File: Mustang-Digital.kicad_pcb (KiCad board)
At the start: 2 copper layers, 67 x 93.3 mm, 100 parts, among them J302 Conn_01x02_Socket, J303 2130830005, J7 Conn_02x08_Odd_Even, J8 Conn_02x08_Odd_Even, U1 BM83SM1-00TB, U2 LP5012RUKR, U301 SPU03L-05, U302 SPU03L-05, U303 SPU03L-05, U304 ADUM4160BRWZ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

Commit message: 3D models.
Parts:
- added J1: 685119248123, Mustang_Library:685119248123, F.Cu at (107.0, 42.7)
- added J2: 685119248123, Mustang_Library:685119248123, F.Cu at (94.2, 42.7)
- C142, C143, C144, C145, D1, D2, D3, D4, D5, D6, D7, D8, U2: moved to B.Cu
- moved J7 223.4 mm to (93.0, 82.2)
- moved U301 223.4 mm to (138.2, 110.1)
- moved C301 223.4 mm to (121.3, 111.0)
- moved C302 223.4 mm to (124.3, 111.0)
- moved C303 223.4 mm to (122.7, 92.3)
- moved C310 223.4 mm to (136.8, 88.0)
- moved C311 223.4 mm to (144.3, 88.0)
- moved L302 223.4 mm to (136.8, 91.0)
- moved L303 223.4 mm to (144.3, 91.0)
- moved R303 223.4 mm to (126.7, 89.8)
- moved R304 223.4 mm to (129.7, 89.8)
- moved R307 223.4 mm to (122.7, 89.3)
- moved R308 223.4 mm to (122.7, 86.3)
- moved S1 223.4 mm to (95.3, 66.8)
- moved S3 223.4 mm to (140.7, 47.2)
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
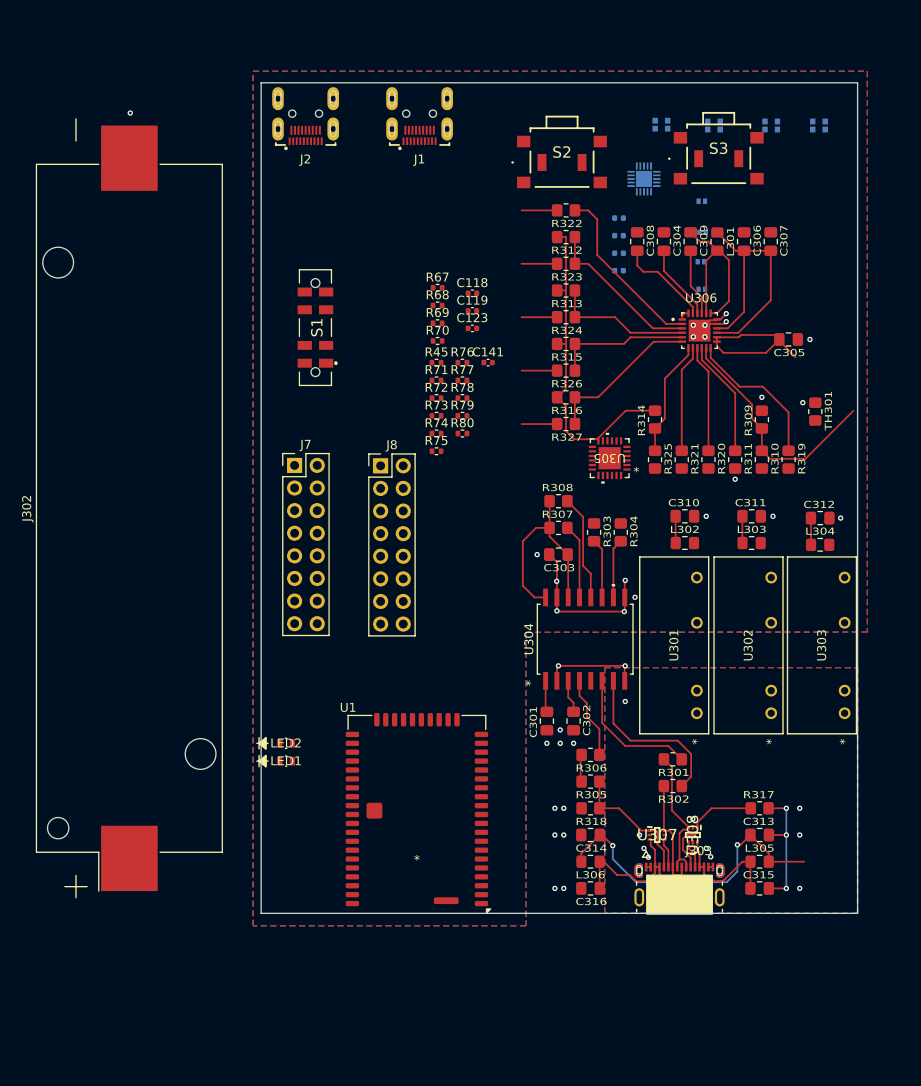
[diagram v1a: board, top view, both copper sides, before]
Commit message: Place and align PCB components to enclosure DXF. Expand PCB 15mm both sides of USB-C. Move BM83 to right side. Cutout PCB along right side for antenna function.
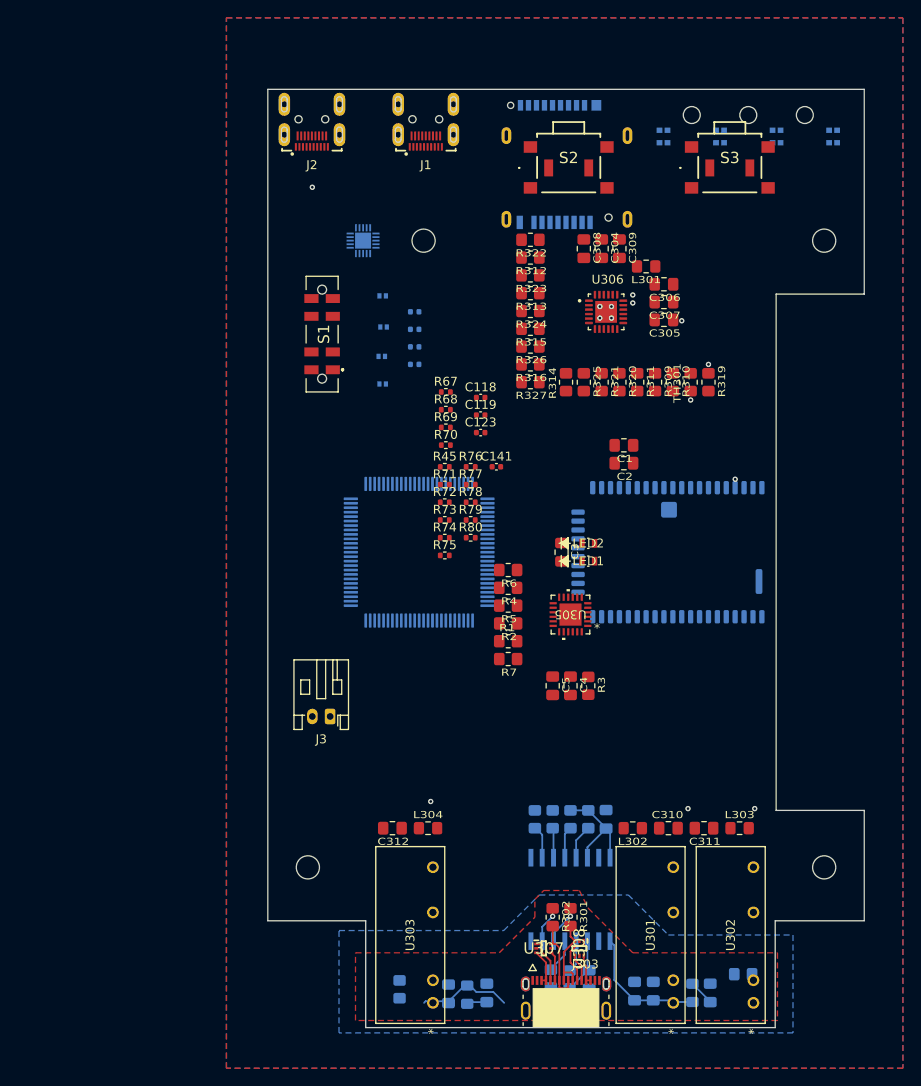
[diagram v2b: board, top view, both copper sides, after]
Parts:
- removed J302: Conn_01x02_Socket, Mustang_Library:BatteryHolder_Keystone_1042_1x18650
- removed J7, J8: Conn_02x08_Odd_Even, Connector_PinHeader_2.54mm:PinHeader_2x08_P2.54mm_Vertical
- added C1: 0.1uF, Mustang_Library:C_0805_2012Metric_Pad1.18x1.45mm_HandSolder, F.Cu at (130.0, 80.0)
- added C2: 1uF, Mustang_Library:C_0805_2012Metric_Pad1.18x1.45mm_HandSolder, F.Cu at (130.0, 82.0)
- added C3: 1uF, Mustang_Library:C_0805_2012Metric_Pad1.18x1.45mm_HandSolder, F.Cu at (123.0, 92.0)
- added C4: 18pF, Mustang_Library:C_0805_2012Metric_Pad1.18x1.45mm_HandSolder, F.Cu at (124.0, 107.0)
- added C5: 18pF, Mustang_Library:C_0805_2012Metric_Pad1.18x1.45mm_HandSolder, F.Cu at (122.0, 107.0)
- added J3: Conn_01x02_Pin, Mustang_Library:JST_PH_S2B-PH-K_1x02_P2.00mm_Horizontal, F.Cu at (97.0, 110.5)
- added J4: Micro_SD_Card_4.0_CUI, Mustang_Library:microSD_XC_CUI_MSD4-1-A, B.Cu at (123.6, 45.2)
- added MECH1: Light_Pipe_LEDs, Mustang_Library:Light_Pipe_LEDs, B.Cu at (144.0, 37.4)
- added MH1: Mounting_Holes, Mustang_Library:Mounting_Holes, F.Cu at (90.0, 40.0)
- added R1: 100k, Mustang_Library:R_0805_2012Metric_Pad1.20x1.40mm_HandSolder, F.Cu at (117.0, 102.0)
- added R2: 100k, Mustang_Library:R_0805_2012Metric_Pad1.20x1.40mm_HandSolder, F.Cu at (117.0, 100.0)
- added R3: 12k, Mustang_Library:R_0805_2012Metric_Pad1.20x1.40mm_HandSolder, F.Cu at (126.0, 107.0)
- added R4: 24R, Mustang_Library:R_0805_2012Metric_Pad1.20x1.40mm_HandSolder, F.Cu at (117.0, 96.0)
- added R5: 24R, Mustang_Library:R_0805_2012Metric_Pad1.20x1.40mm_HandSolder, F.Cu at (117.0, 98.0)
- added R6: 24R, Mustang_Library:R_0805_2012Metric_Pad1.20x1.40mm_HandSolder, F.Cu at (117.0, 94.0)
- added R7: 24R, Mustang_Library:R_0805_2012Metric_Pad1.20x1.40mm_HandSolder, F.Cu at (117.0, 104.0)
- added U3: STM32L496VGTx, Mustang_Library:LQFP-100_14x14mm_P0.5mm, B.Cu at (107.0, 92.0)
- C301, C302, C303, C313, C314, C315, C316, L305, L306, R303, R304, R305, R306, R307, R308, R317, R318, U1, U304: moved to B.Cu
- moved C312 59.3 mm to (104.0, 123.0), turned to 0 degrees
- moved U303 56.5 mm to (108.5, 142.6)
- moved L304 54.3 mm to (108.0, 123.0)
- moved U1 48.4 mm to (140.6, 92.0), turned to 90 degrees
- moved LED1 40.7 mm to (126.0, 93.0)
- moved LED2 40.7 mm to (126.0, 91.0)
- moved D7 37.4 mm to (102.8, 70.0)
- moved D1 37.4 mm to (102.9, 63.2)
- moved D2 37.4 mm to (103.0, 66.7)
- moved D8 37.4 mm to (102.9, 73.1)
- moved R308 35.8 mm to (124.0, 122.0), turned to 90 degrees
- moved C311 35.4 mm to (139.0, 123.0), turned to 0 degrees
- moved C310 35.1 mm to (135.0, 123.0)
- moved R304 33.6 mm to (120.0, 122.0)
- moved R307 32.9 mm to (126.0, 122.0), turned to 90 degrees
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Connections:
- net /Charging_Isolation/UCE renamed /Charging_Isolation/BQCE
- net /Charging_Isolation/UINT renamed /Charging_Isolation/BQINT
- net /Charging_Isolation/UOTG renamed /Charging_Isolation/BQOTG
- net /Charging_Isolation/UPG renamed /Charging_Isolation/BQPG
- net /Charging_Isolation/UPSEL renamed /Charging_Isolation/BQPSEL
- net /Charging_Isolation/UQON renamed /Charging_Isolation/BQQON
- net /Charging_Isolation/USTAT renamed /Charging_Isolation/BQSTAT
- net /Charging_Isolation/VBUS-U6 renamed /Charging_Isolation/VBUS-ISO
- net /Charging_Isolation//OCS1 renamed /Charging_Isolation/OCS1_N
- net /Charging_Isolation//OCS2 renamed /Charging_Isolation/OCS2_N
- J303 pad SH1: Earth -> GNDPWR
- J303 pad SH2: Earth -> GNDPWR
- J303 pad SH3: Earth -> GNDPWR
- J303 pad SH4: Earth -> GNDPWR
- R315 pad 2: /Charging_Isolation/SCL -> /Charging_Isolation/_SCL
- R316 pad 2: /Charging_Isolation/SDA -> /Charging_Isolation/_SDA
- R326 pad 1: /Charging_Isolation/USCL -> /Charging_Isolation/SCL
- R326 pad 2: /Charging_Isolation/SCL -> /Charging_Isolation/_SCL
- R327 pad 1: /Charging_Isolation/USDA -> /Charging_Isolation/SDA
- R327 pad 2: /Charging_Isolation/SDA -> /Charging_Isolation/_SDA
- U305 pad 15: /Charging_Isolation//RESET -> /Charging_Isolation/_RESET_N
- U305 pad 17: /Charging_Isolation/SUSP -> /Charging_Isolation/SUSP_IND
- U305 pad 25: /Charging_Isolation/EPAD -> GND
- U306 pad 5: /Charging_Isolation/SCL -> /Charging_Isolation/_SCL
- U306 pad 6: /Charging_Isolation/SDA -> /Charging_Isolation/_SDA
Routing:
- net /Charging_Isolation/3V3: track 60.7 -> 12.5 mm
- net /Charging_Isolation/VSYS: track 30.7 -> 0.00 mm
- net /Charging_Isolation/TS: track 27.1 -> 0.00 mm
- net GNDPWR: track 26.6 -> 0.00 mm, vias 25 -> 0
- net GND: track 25.0 -> 0.00 mm, vias 20 -> 12
- net /Charging_Isolation/VBUS0: track 35.0 -> 12.6 mm
- net /Charging_Isolation/SW: track 20.4 -> 0.00 mm
- net /Charging_Isolation/PSEL: track 19.7 -> 0.00 mm
- net /Charging_Isolation/BAT: track 19.0 -> 0.00 mm
- net /Charging_Isolation/PG: track 18.1 -> 0.00 mm
- net /Charging_Isolation/SDA: track 17.7 -> 0.00 mm
- net /Charging_Isolation/QON: track 16.7 -> 0.00 mm, vias 0 -> 1
- net /Charging_Isolation/STAT: track 15.8 -> 0.00 mm
- net /Charging_Isolation/SCL: track 15.4 -> 0.00 mm
- net /Charging_Isolation/UD+: track 19.0 -> 4.17 mm, vias 0 -> 1
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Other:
- board size 67 x 93.3 mm -> 67 x 105.4 mm

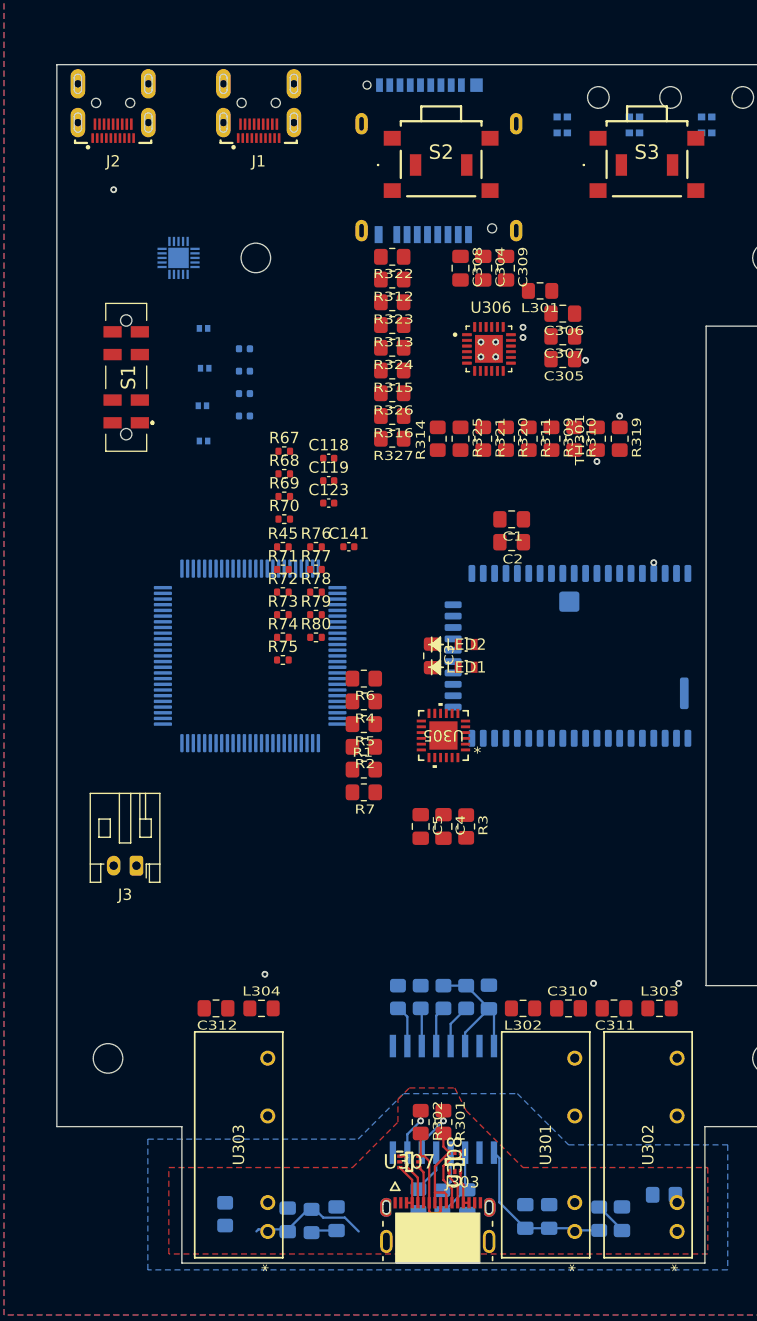
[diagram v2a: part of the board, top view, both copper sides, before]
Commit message: Footprint inspections and cleanups.
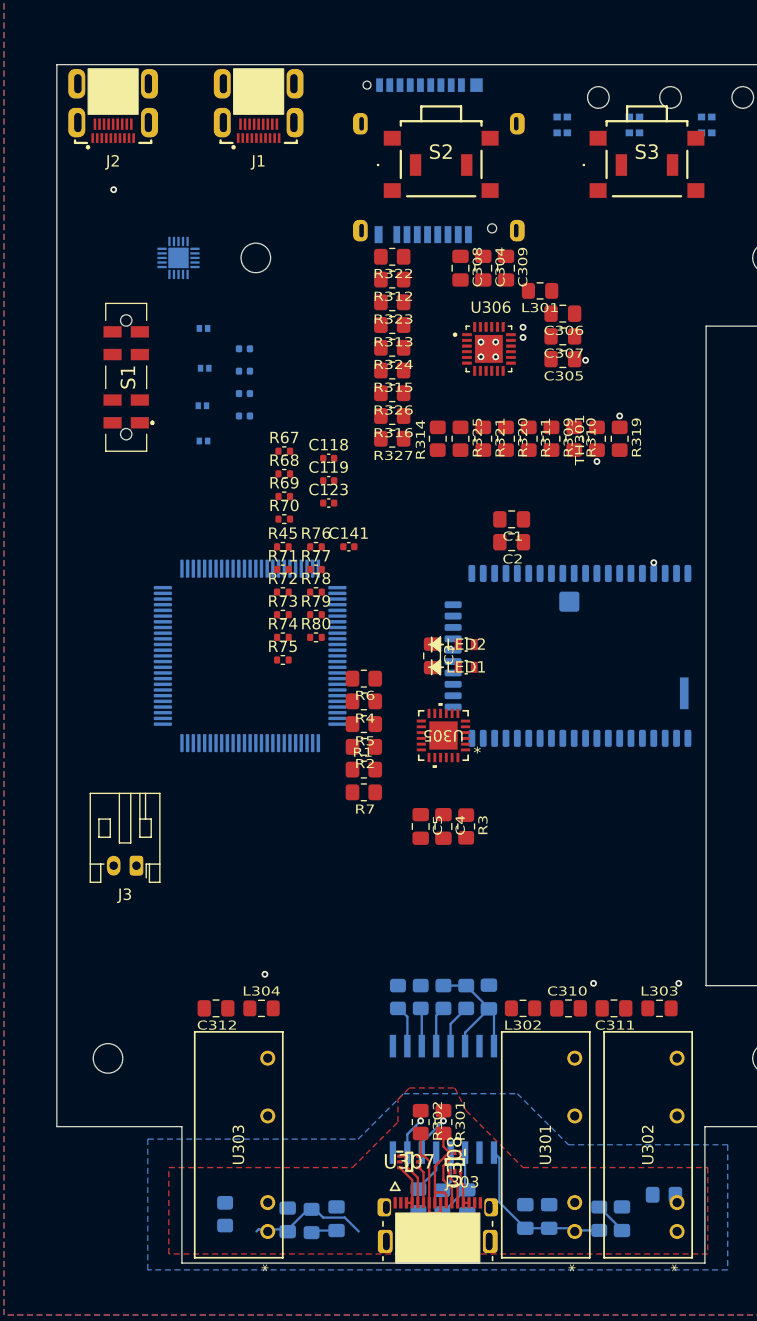
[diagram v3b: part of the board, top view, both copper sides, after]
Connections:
- net LED SCL renamed LEDSCL
- C141 pad 1: GNDD -> GND
- C142 pad 1: GNDD -> GND
- C143 pad 1: GNDD -> GND
- C144 pad 1: GNDD -> GND
- C145 pad 1: GNDD -> GND
- D1 pad 1: GNDD -> GND
- D2 pad 1: GNDD -> GND
- D7 pad 1: GNDD -> GND
- D8 pad 1: GNDD -> GND
- J1 pad S1: unconnected-(J1-SHIELD-PadS1) -> GND
- J1 pad S2: unconnected-(J1-SHIELD__1-PadS2) -> GND
- J1 pad S3: unconnected-(J1-SHIELD__2-PadS3) -> GND
- J1 pad S4: unconnected-(J1-SHIELD__3-PadS4) -> GND
- J2 pad S1: unconnected-(J2-SHIELD-PadS1) -> GND
- J2 pad S2: unconnected-(J2-SHIELD__1-PadS2) -> GND
- J2 pad S3: unconnected-(J2-SHIELD__2-PadS3) -> GND
- J2 pad S4: unconnected-(J2-SHIELD__3-PadS4) -> GND
- R76 pad 2: GNDD -> GND
- S1 pad 1: GNDD -> GND
- S1 pad 2: GNDD -> GND
- S1 pad 7: GNDD -> GND
- S2 pad 2: GNDD -> GND
- S2 pad MP1: unconnected-(S2-PadMP1) -> GND
- S2 pad MP2: unconnected-(S2-PadMP2) -> GND
- S2 pad MP3: unconnected-(S2-PadMP3) -> GND
- S2 pad MP4: unconnected-(S2-PadMP4) -> GND
- S3 pad 2: GNDD -> GND
- U2 pad 14: GNDD -> GND
- U2 pad 15: GNDD -> GND
- U2 pad 21: GNDD -> GND

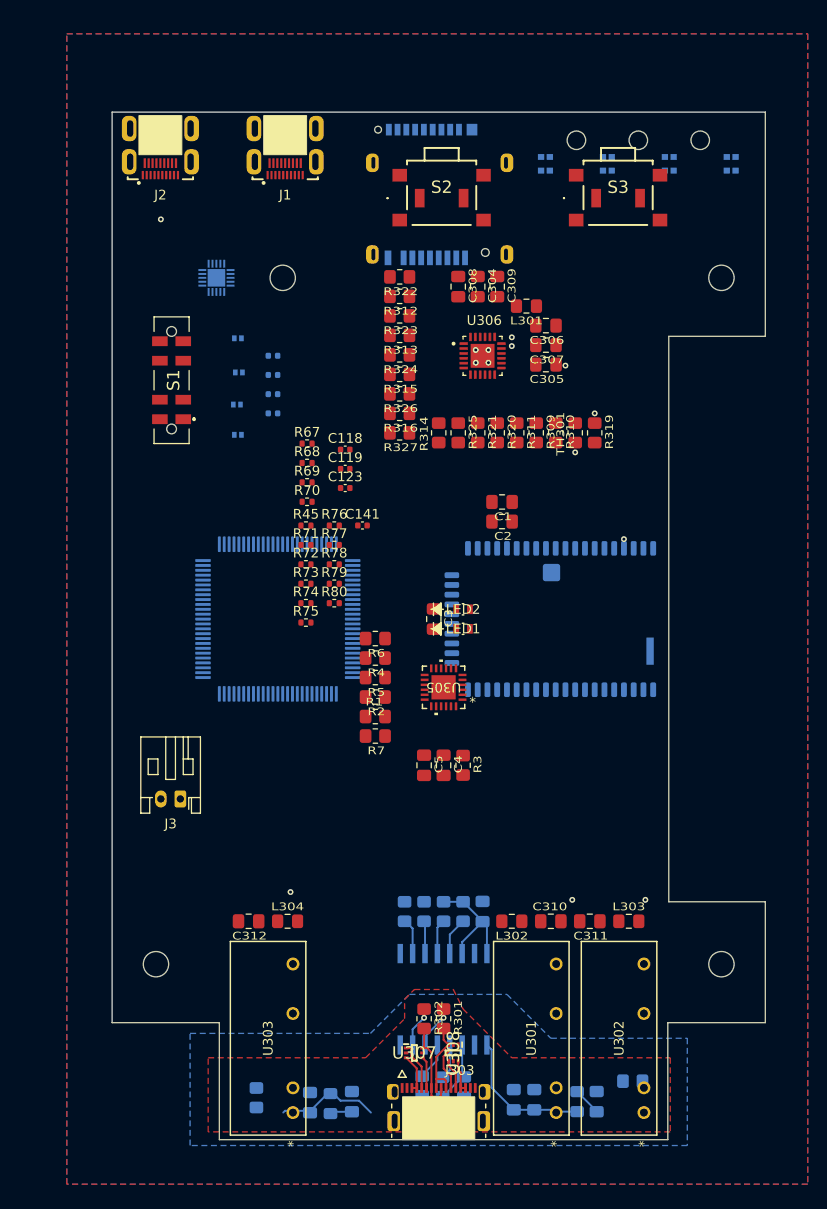
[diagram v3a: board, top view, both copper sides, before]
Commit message: Add extra mounting hole. Relocate BM83 per Juan.
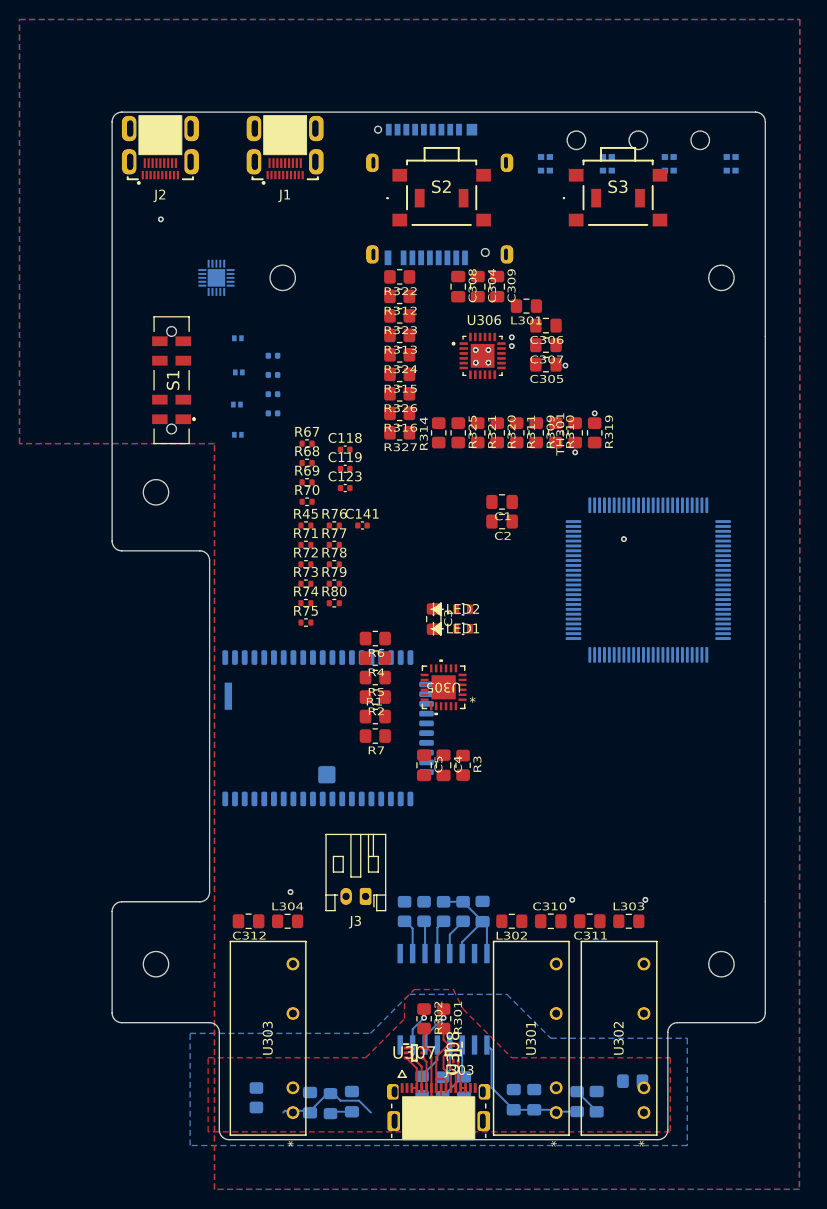
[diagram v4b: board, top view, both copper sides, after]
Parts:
- added ?: , , F.Cu at (94.5, 79.0)
- moved U3 38.2 mm to (145.0, 88.0)
- moved U1 35.9 mm to (106.5, 103.2), turned to -90 degrees
- moved J3 21.5 mm to (116.0, 120.5)
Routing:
- added copper zone on In1.Cu, net GND
- added copper zone on In2.Cu, net GND
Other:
- outline, holes or cut-outs redrawn
- copper layers 2 -> 4
- rule pad_to_mask_clearance: 0 -> 0.1016
